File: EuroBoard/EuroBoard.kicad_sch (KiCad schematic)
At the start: 33 parts, among them J1 GPIO, J10 PD1, J11 PD2, J12 PD3, J2 Conn_01x07_Male, J3 I2C, J4 Conn_01x05_Male, J5 RX, J6 TX, J7 GND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

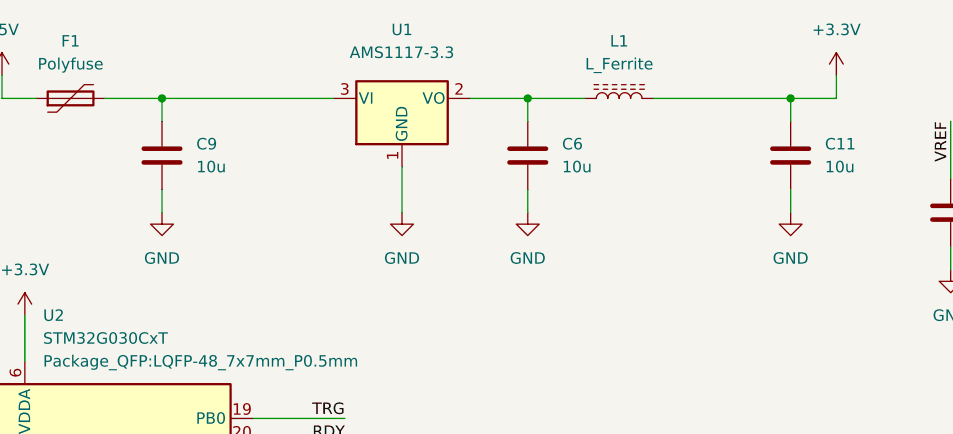
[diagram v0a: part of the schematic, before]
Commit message: Added alectrolytic capacitors
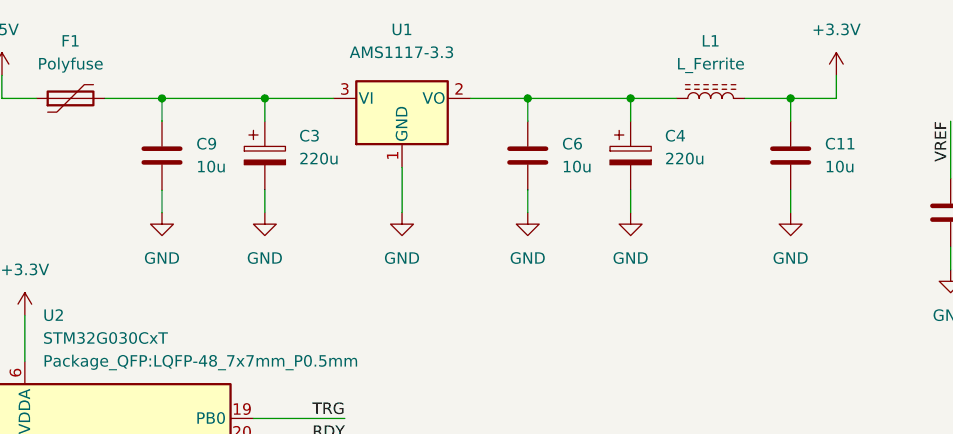
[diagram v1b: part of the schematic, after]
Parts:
- added C3, C4: 220u, Capacitor_SMD:CP_Elec_6.3x7.7, symbol Device:C_Polarized
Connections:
- net GND: now also C3.2, C4.2
- net at C6.1, L1.1, U1.2 (VO): now also C4.1
- net at C9.1, F1.2, U1.3 (VI): now also C3.1
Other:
- moved on the sheet: L1
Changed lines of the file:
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@@
   (junction (at 110.49 64.77) (diameter 0) (color 0 0 0 0)
   )
+  (junction (at 232.41 22.86) (diameter 0) (color 0 0 0 0)
+  )
   (junction (at 40.64 59.69) (diameter 0) (color 0 0 0 0)
   )
   (junction (at 102.87 64.77) (diameter 0) (color 0 0 0 0)
   )
+  (junction (at 173.99 22.86) (diameter 0) (color 0 0 0 0)
+  )
   (junction (at 210.82 99.06) (diameter 0) (color 0 0 0 0)
   )
   (junction (at 66.04 152.4) (diameter 0) (color 0 0 0 0)
   )
-  (junction (at 232.41 22.86) (diameter 0) (color 0 0 0 0)
+  (junction (at 214.63 22.86) (diameter 0) (color 0 0 0 0)
   )
   (junction (at 50.8 66.04) (diameter 0) (color 0 0 0 0)
@@
     (stroke (width 0) (type default) (color 0 0 0 0))
   )
+  (wire (pts (xy 173.99 22.86) (xy 173.99 25.4))
+    (stroke (width 0) (type default) (color 0 0 0 0))
+  )
   (wire (pts (xy 248.92 111.76) (xy 246.38 111.76))
     (stroke (width 0) (type default) (color 0 0 0 0))
@@
     (stroke (width 0) (type default) (color 0 0 0 0))
   )
+  (wire (pts (xy 227.33 22.86) (xy 232.41 22.86))
+    (stroke (width 0) (type default) (color 0 0 0 0))
+  )
   (wire (pts (xy 40.64 59.69) (xy 40.64 62.23))
     (stroke (width 0) (type default) (color 0 0 0 0))
@@
     (stroke (width 0) (type default) (color 0 0 0 0))
   )
-  (wire (pts (xy 217.17 22.86) (xy 232.41 22.86))
-    (stroke (width 0) (type default) (color 0 0 0 0))
-  )
   (wire (pts (xy 50.8 64.77) (xy 50.8 66.04))
     (stroke (width 0) (type default) (color 0 0 0 0))
@@
     (stroke (width 0) (type default) (color 0 0 0 0))
   )
+  (wire (pts (xy 173.99 33.02) (xy 173.99 35.56))
+    (stroke (width 0) (type default) (color 0 0 0 0))
+  )
   (wire (pts (xy 208.28 91.44) (xy 210.82 91.44))
     (stroke (width 0) (type default) (color 0 0 0 0))
@@
     (stroke (width 0) (type default) (color 0 0 0 0))
   )
+  (wire (pts (xy 214.63 22.86) (xy 219.71 22.86))
+    (stroke (width 0) (type default) (color 0 0 0 0))
+  )
   (wire (pts (xy 66.04 152.4) (xy 67.31 152.4))
     (stroke (width 0) (type default) (color 0 0 0 0))
@@
     (stroke (width 0) (type default) (color 0 0 0 0))
   )
-  (wire (pts (xy 162.56 22.86) (xy 181.61 22.86))
+  (wire (pts (xy 162.56 22.86) (xy 173.99 22.86))
     (stroke (width 0) (type default) (color 0 0 0 0))
   )
@@
     (stroke (width 0) (type default) (color 0 0 0 0))
   )
-  (wire (pts (xy 203.2 22.86) (xy 209.55 22.86))
+  (wire (pts (xy 203.2 22.86) (xy 214.63 22.86))
     (stroke (width 0) (type default) (color 0 0 0 0))
   )
@@
     (stroke (width 0) (type default) (color 0 0 0 0))
   )
+  (wire (pts (xy 214.63 22.86) (xy 214.63 25.4))
+    (stroke (width 0) (type default) (color 0 0 0 0))
+  )
   (wire (pts (xy 72.39 167.64) (xy 64.77 167.64))
     (stroke (width 0) (type default) (color 0 0 0 0))
@@
     (stroke (width 0) (type default) (color 0 0 0 0))
   )
+  (wire (pts (xy 214.63 33.02) (xy 214.63 35.56))
+    (stroke (width 0) (type default) (color 0 0 0 0))
+  )
   (wire (pts (xy 210.82 96.52) (xy 210.82 99.06))
     (stroke (width 0) (type default) (color 0 0 0 0))
@@
   )
   (wire (pts (xy 246.38 88.9) (xy 254 88.9))
+    (stroke (width 0) (type default) (color 0 0 0 0))
+  )
+  (wire (pts (xy 173.99 22.86) (xy 181.61 22.86))
     (stroke (width 0) (type default) (color 0 0 0 0))
   )
@@
     )
     (pin "1")
+  )
+  (symbol (lib_id "Device:C_Polarized") (at 214.63 29.21 0) (unit 1)
+    (in_bom yes) (on_board yes) (fields_autoplaced)
+    (property "Reference" "C4" (id 0) (at 218.44 27.0509 0)
+      (effects (font (size 1.27 1.27)) (justify left))
+    )
+    (property "Value" "220u" (id 1) (at 218.44 29.5909 0)
+      (effects (font (size 1.27 1.27)) (justify left))
+    )
+    (property "Footprint" "Capacitor_SMD:CP_Elec_6.3x7.7" (id 2) (at 215.5952 33.02 0)
+      (effects (font (size 1.27 1.27)) hide)
+    )
+    (property "Datasheet" "~" (id 3) (at 214.63 29.21 0)
+      (effects (font (size 1.27 1.27)) hide)
+    )
+    (pin "1")
+    (pin "2")
   )
   (symbol (lib_id "Device:R") (at 45.72 92.71 180) (unit 1)
@@
     (pin "1")
   )
+  (symbol (lib_id "Device:C_Polarized") (at 173.99 29.21 0) (unit 1)
+    (in_bom yes) (on_board yes) (fields_autoplaced)
+    (property "Reference" "C3" (id 0) (at 177.8 27.0509 0)
+      (effects (font (size 1.27 1.27)) (justify left))
+    )
+    (property "Value" "220u" (id 1) (at 177.8 29.5909 0)
+      (effects (font (size 1.27 1.27)) (justify left))
+    )
+    (property "Footprint" "Capacitor_SMD:CP_Elec_6.3x7.7" (id 2) (at 174.9552 33.02 0)
+      (effects (font (size 1.27 1.27)) hide)
+    )
+    (property "Datasheet" "~" (id 3) (at 173.99 29.21 0)
+      (effects (font (size 1.27 1.27)) hide)
+    )
+    (pin "1")
+    (pin "2")
+  )
   (symbol (lib_id "power:+12V") (at 72.39 147.32 270) (unit 1)
     (in_bom yes) (on_board yes) (fields_autoplaced)
@@
     (pin "6")
     (pin "7")
+  )
+  (symbol (lib_id "power:GND") (at 173.99 35.56 0) (unit 1)
+    (in_bom yes) (on_board yes) (fields_autoplaced)
+    (property "Reference" "#PWR0109" (id 0) (at 173.99 41.91 0)
+      (effects (font (size 1.27 1.27)) hide)
+    )
+    (property "Value" "GND" (id 1) (at 173.99 40.64 0))
+    (property "Footprint" "" (id 2) (at 173.99 35.56 0)
+      (effects (font (size 1.27 1.27)) hide)
+    )
+    (property "Datasheet" "" (id 3) (at 173.99 35.56 0)
+      (effects (font (size 1.27 1.27)) hide)
+    )
+    (pin "1")
   )
   (symbol (lib_id "Device:C") (at 162.56 29.21 0) (unit 1)
@@
     (pin "2")
   )
-  (symbol (lib_id "Device:L_Ferrite") (at 213.36 22.86 90) (unit 1)
-    (in_bom yes) (on_board yes) (fields_autoplaced)
-    (property "Reference" "L1" (id 0) (at 213.36 16.51 90))
-    (property "Value" "L_Ferrite" (id 1) (at 213.36 19.05 90))
-    (property "Footprint" "Inductor_SMD:L_0805_2012Metric_Pad1.15x1.40mm_HandSolder" (id 2) (at 213.36 22.86 0)
-      (effects (font (size 1.27 1.27)) hide)
-    )
-    (property "Datasheet" "~" (id 3) (at 213.36 22.86 0)
+  (symbol (lib_id "Device:L_Ferrite") (at 223.52 22.86 90) (unit 1)
+    (in_bom yes) (on_board yes) (fields_autoplaced)
+    (property "Reference" "L1" (id 0) (at 223.52 16.51 90))
+    (property "Value" "L_Ferrite" (id 1) (at 223.52 19.05 90))
+    (property "Footprint" "Inductor_SMD:L_0805_2012Metric_Pad1.15x1.40mm_HandSolder" (id 2) (at 223.52 22.86 0)
+      (effects (font (size 1.27 1.27)) hide)
+    )
+    (property "Datasheet" "~" (id 3) (at 223.52 22.86 0)
       (effects (font (size 1.27 1.27)) hide)
     )
@@
     )
     (property "Datasheet" "" (id 3) (at 43.18 139.7 0)
+      (effects (font (size 1.27 1.27)) hide)
+    )
+    (pin "1")
+  )
+  (symbol (lib_id "power:GND") (at 214.63 35.56 0) (unit 1)
+    (in_bom yes) (on_board yes) (fields_autoplaced)
+    (property "Reference" "#PWR0108" (id 0) (at 214.63 41.91 0)
+      (effects (font (size 1.27 1.27)) hide)
+    )
+    (property "Value" "GND" (id 1) (at 214.63 40.64 0))
+    (property "Footprint" "" (id 2) (at 214.63 35.56 0)
+      (effects (font (size 1.27 1.27)) hide)
+    )
+    (property "Datasheet" "" (id 3) (at 214.63 35.56 0)
       (effects (font (size 1.27 1.27)) hide)
     )
@@
       (reference "#PWR0107") (unit 1) (value "+3.3V") (footprint "")
     )
+    (path "/d30d9cc9-5d0b-45af-8d52-ae1dd9a21283"
+      (reference "#PWR0108") (unit 1) (value "GND") (footprint "")
+    )
+    (path "/a34ea007-f1d5-42a3-9fae-4752579b644e"
+      (reference "#PWR0109") (unit 1) (value "GND") (footprint "")
+    )
     (path "/ecb73b8c-3d8b-47f7-ac3c-849a31982412"
       (reference "#PWR0111") (unit 1) (value "+5V") (footprint "")
@@
       (reference "C2") (unit 1) (value "100n") (footprint "Capacitor_SMD:C_0805_2012Metric_Pad1.18x1.45mm_HandSolder")
     )
+    (path "/948bdaf7-fd2a-4d24-9c5d-a68f85739e13"
+      (reference "C3") (unit 1) (value "220u") (footprint "Capacitor_SMD:CP_Elec_6.3x7.7")
+    )
+    (path "/0fc73465-5b23-4a05-967f-ded38547596f"
+      (reference "C4") (unit 1) (value "220u") (footprint "Capacitor_SMD:CP_Elec_6.3x7.7")
+    )
     (path "/af3713c5-ab8e-47d8-9144-f62cbe584e43"

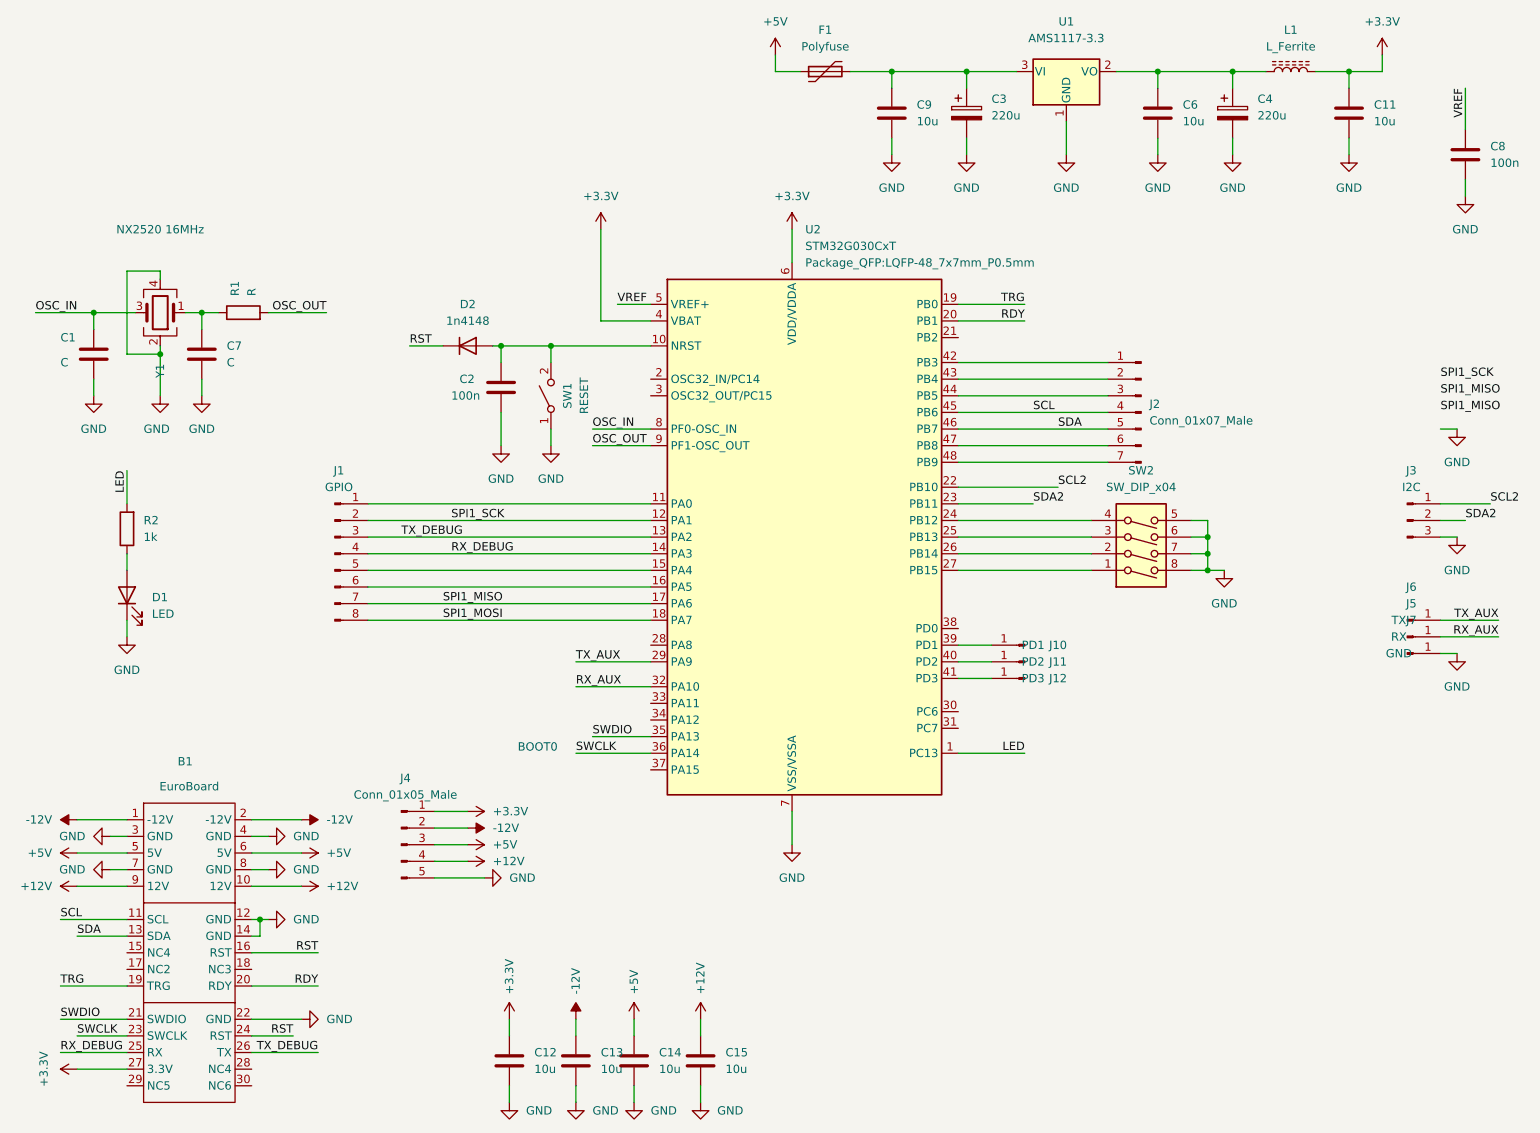
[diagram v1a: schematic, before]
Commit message: Connected free bus lines to GPIO
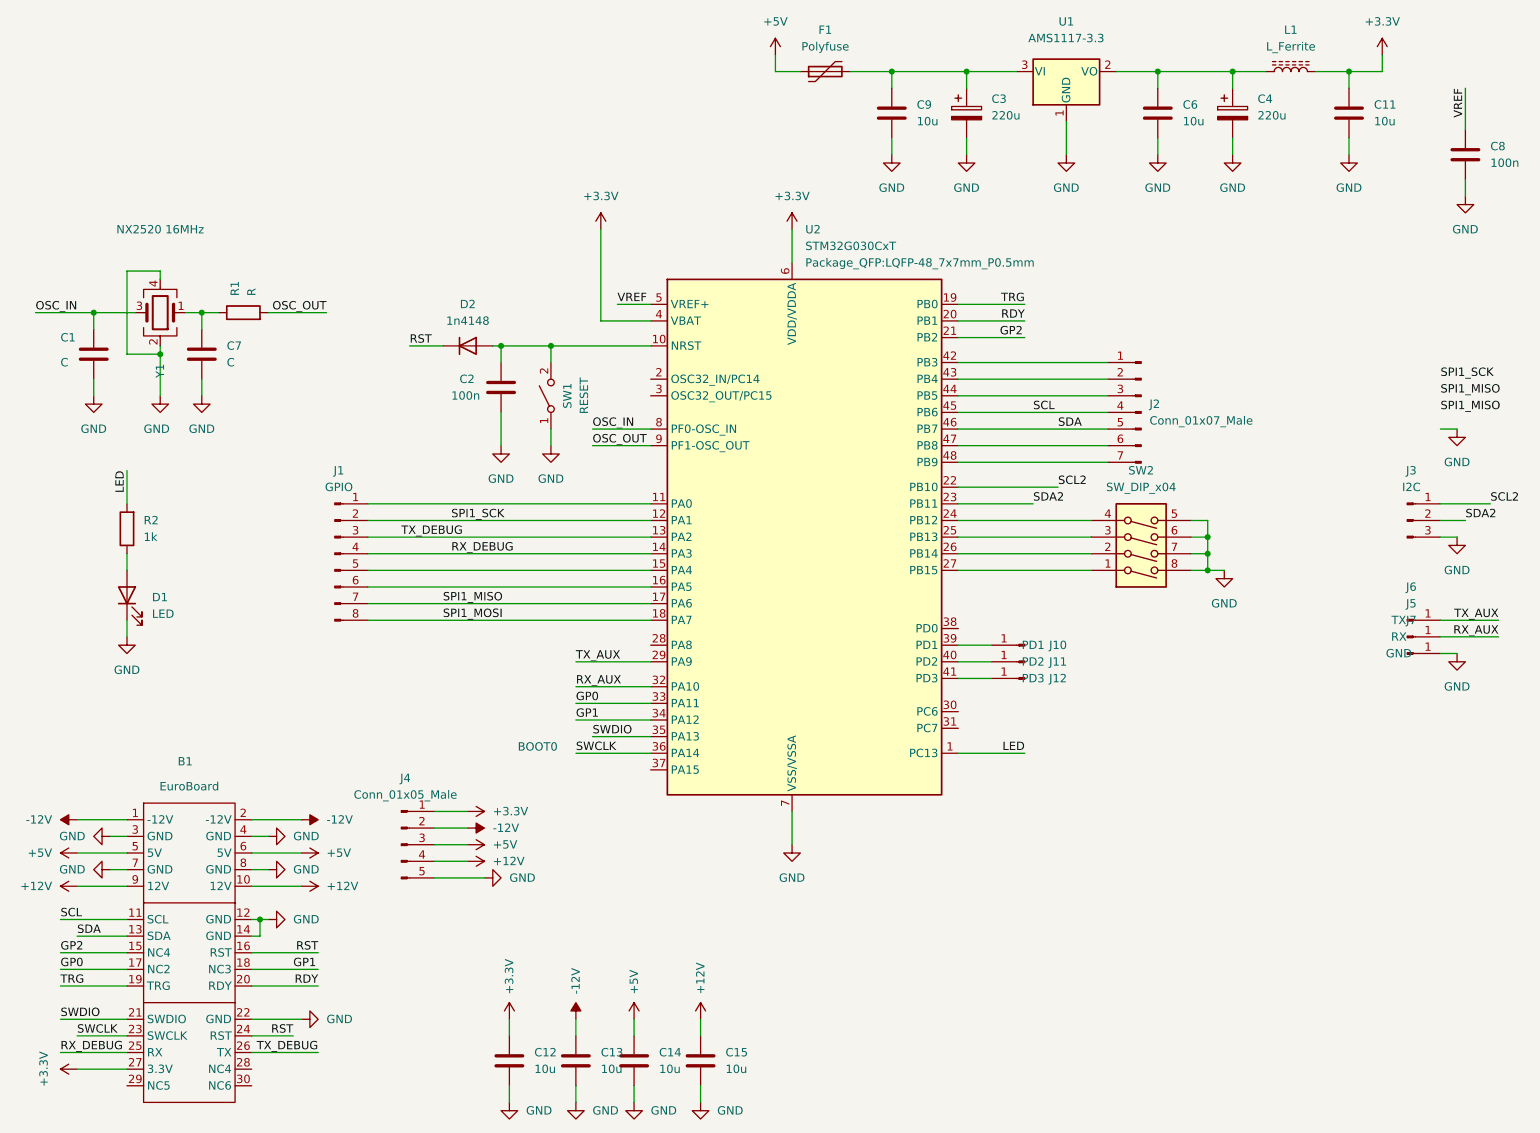
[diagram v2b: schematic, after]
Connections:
- net GP2: now reaches U2.21 (PB2)
- net GP2: now also B1.15 (NC4)
- net GP0: now reaches U2.33 (PA11)
- net GP0: now also B1.17 (NC2)
- net GP1: now reaches U2.34 (PA12)
- net GP1: now also B1.18 (NC3)
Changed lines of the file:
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@@
+    (stroke (width 0) (type default) (color 0 0 0 0))
+  )
+  (wire (pts (xy 172.72 63.5) (xy 182.88 63.5))
     (stroke (width 0) (type default) (color 0 0 0 0))
   )
@@
     (stroke (width 0) (type default) (color 0 0 0 0))
   )
+  (wire (pts (xy 114.3 119.38) (xy 125.73 119.38))
+    (stroke (width 0) (type default) (color 0 0 0 0))
+  )
   (wire (pts (xy 133.35 167.64) (xy 133.35 170.18))
     (stroke (width 0) (type default) (color 0 0 0 0))
@@
     (stroke (width 0) (type default) (color 0 0 0 0))
   )
+  (wire (pts (xy 35.56 160.02) (xy 45.72 160.02))
+    (stroke (width 0) (type default) (color 0 0 0 0))
+  )
+  (wire (pts (xy 64.77 160.02) (xy 74.93 160.02))
+    (stroke (width 0) (type default) (color 0 0 0 0))
+  )
   (wire (pts (xy 92.71 138.43) (xy 97.79 138.43))
     (stroke (width 0) (type default) (color 0 0 0 0))
@@
     (stroke (width 0) (type default) (color 0 0 0 0))
   )
+  (wire (pts (xy 35.56 157.48) (xy 45.72 157.48))
+    (stroke (width 0) (type default) (color 0 0 0 0))
+  )
   (wire (pts (xy 144.78 22.86) (xy 148.59 22.86))
     (stroke (width 0) (type default) (color 0 0 0 0))
@@
     (stroke (width 0) (type default) (color 0 0 0 0))
   )
+  (wire (pts (xy 114.3 121.92) (xy 125.73 121.92))
+    (stroke (width 0) (type default) (color 0 0 0 0))
+  )
   (wire (pts (xy 210.82 93.98) (xy 210.82 96.52))
     (stroke (width 0) (type default) (color 0 0 0 0))
@@
     (effects (font (size 1.27 1.27)) (justify left bottom))
   )
+  (label "GP2" (at 35.56 157.48 0)
+    (effects (font (size 1.27 1.27)) (justify left bottom))
+  )
+  (label "GP2" (at 179.07 63.5 0)
+    (effects (font (size 1.27 1.27)) (justify left bottom))
+  )
   (label "SWDIO" (at 35.56 167.64 0)
     (effects (font (size 1.27 1.27)) (justify left bottom))
@@
     (effects (font (size 1.27 1.27)) (justify right bottom))
   )
+  (label "GP1" (at 114.3 121.92 0)
+    (effects (font (size 1.27 1.27)) (justify left bottom))
+  )
   (label "SWCLK" (at 38.1 170.18 0)
     (effects (font (size 1.27 1.27)) (justify left bottom))
@@
     (effects (font (size 1.27 1.27)) (justify left bottom))
   )
+  (label "GP0" (at 35.56 160.02 0)
+    (effects (font (size 1.27 1.27)) (justify left bottom))
+  )
   (label "RX_AUX" (at 114.3 116.84 0)
     (effects (font (size 1.27 1.27)) (justify left bottom))
@@
     (effects (font (size 1.27 1.27)) (justify left bottom))
   )
+  (label "GP0" (at 114.3 119.38 0)
+    (effects (font (size 1.27 1.27)) (justify left bottom))
+  )
   (label "RDY" (at 74.93 162.56 180)
     (effects (font (size 1.27 1.27)) (justify right bottom))
   )
+  (label "GP1" (at 71.12 160.02 0)
+    (effects (font (size 1.27 1.27)) (justify left bottom))
+  )
   (label "OSC_OUT" (at 76.2 59.69 180)
